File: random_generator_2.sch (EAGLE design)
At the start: 17 parts, among them IC1 OPA2340U

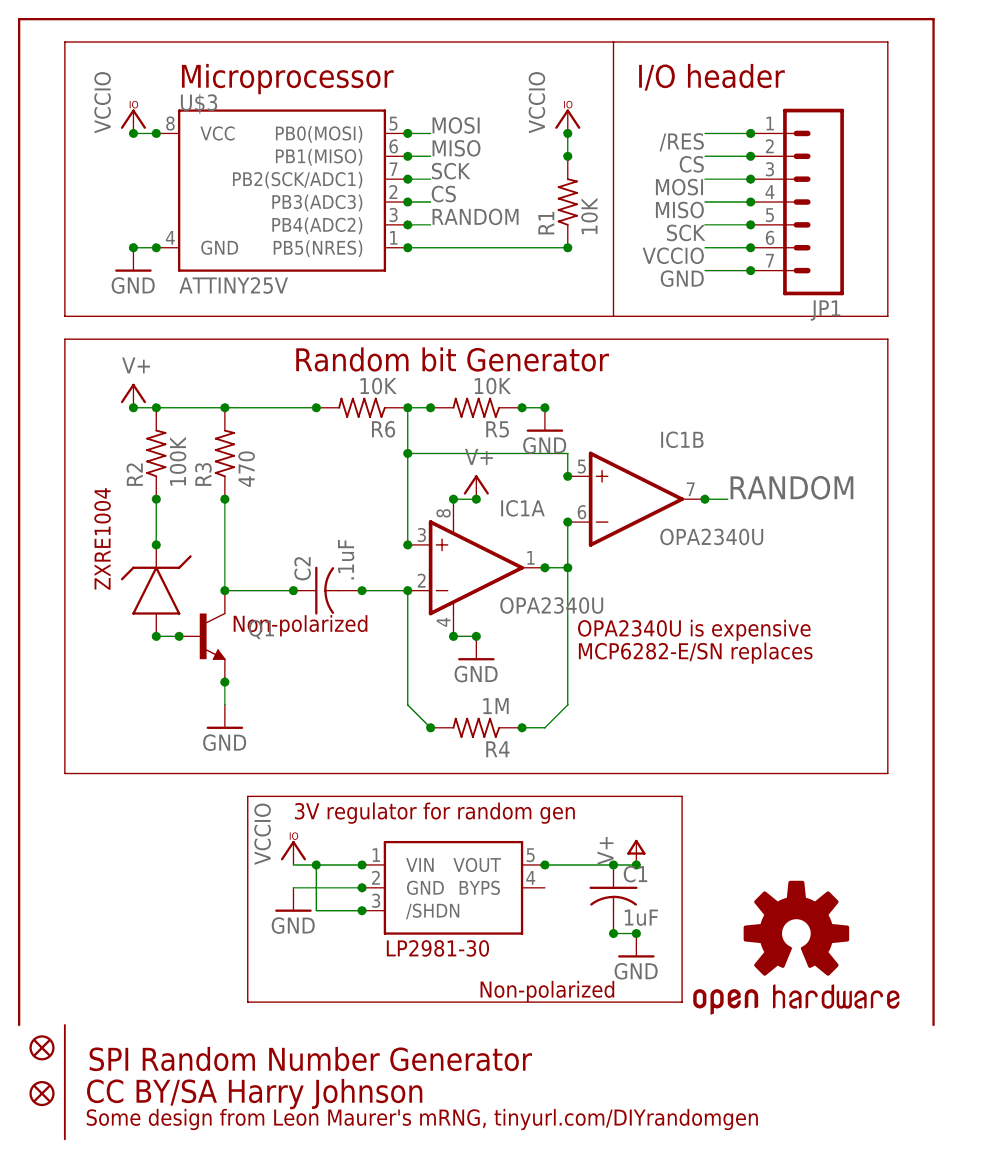
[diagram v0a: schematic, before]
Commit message: MANY BUGS! NOW, HANDLE IT!
A whole nightmarish mess of bugs fixed: Dr Nyquist prescribed some
faster sampling, (just in case). I also tied op amp to VCCIO instead of
3V (for voltage swings guaranteed to trigger logic high), SPI/USI code
now works too. WIll upload an Arduino test program soon…
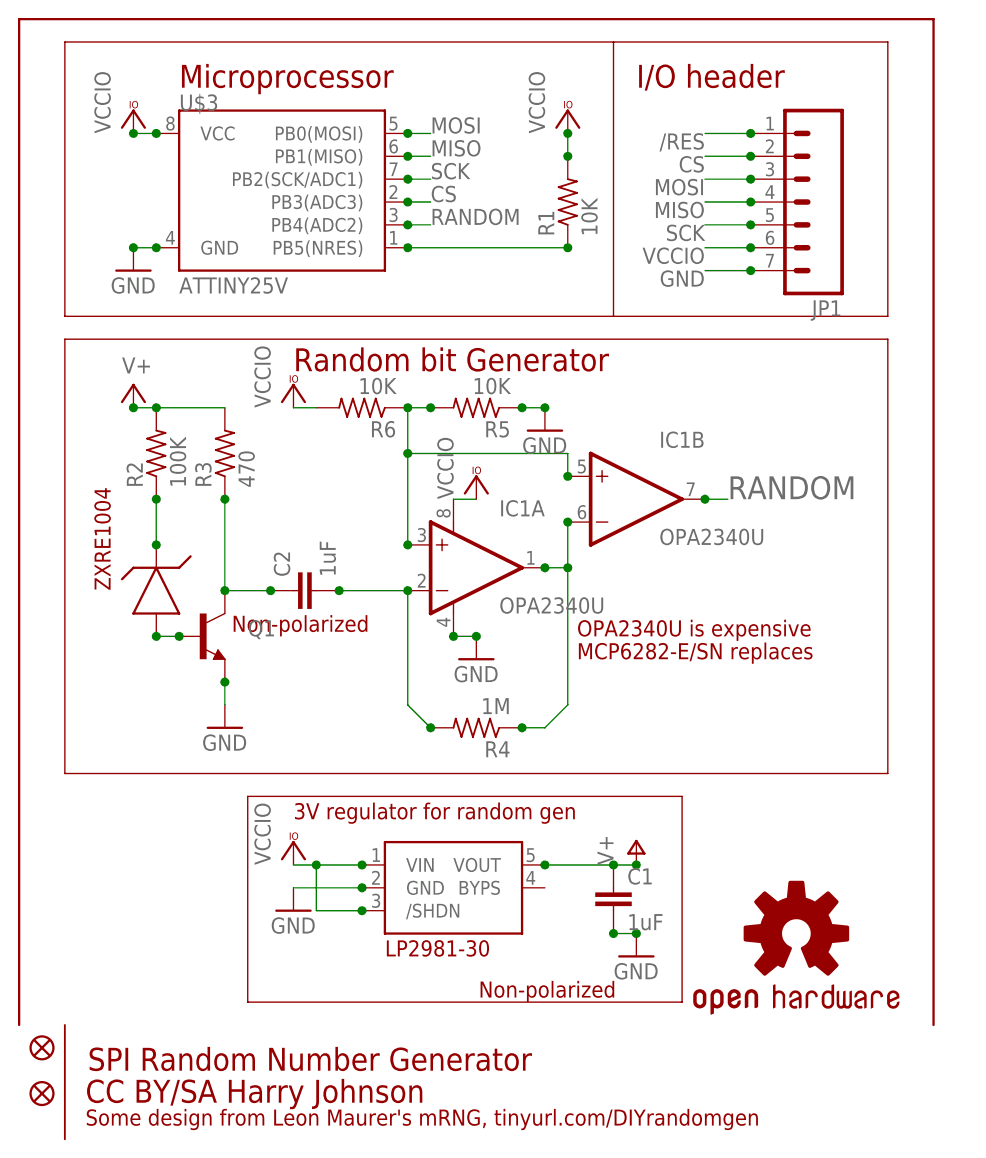
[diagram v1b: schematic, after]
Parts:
- C1: device adafruit:C-USC0805 -> SparkFun:CAP0805
- C2: value .1uF -> 1uF; device adafruit:C-USC0805 -> SparkFun:CAP0805
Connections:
- net V+: no longer IC1A.V+, R6.2
- net VCCIO: now also IC1A.V+, R6.2
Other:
- moved on the sheet: C2
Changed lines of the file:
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@@
 <part name="R5" library="adafruit" deviceset="R-US_" device="R0805" value="10K"/>
 <part name="R6" library="adafruit" deviceset="R-US_" device="R0805" value="10K"/>
-<part name="C2" library="adafruit" deviceset="C-US" device="C0805" value=".1uF"/>
+<part name="C2" library="SparkFun" deviceset="CAP" device="0805" value="1uF"/>
 <part name="SUPPLY1" library="supply2" deviceset="V+" device=""/>
-<part name="SUPPLY2" library="supply2" deviceset="V+" device=""/>
 <part name="U$2" library="hjohnson_library" deviceset="TC1014" device=""/>
-<part name="C1" library="adafruit" deviceset="C-US" device="C0805" value="1uF"/>
+<part name="C1" library="SparkFun" deviceset="CAP" device="0805" value="1uF"/>
 <part name="P+1" library="supply1" deviceset="V+" device=""/>
 <part name="GND1" library="SparkFun" deviceset="GND" device=""/>
@@
 <part name="JP3" library="SparkFun" deviceset="FIDUCIAL" device="UFIDUCIAL"/>
 <part name="U$4" library="SparkFun" deviceset="OSHW-LOGO" device="S"/>
+<part name="VCC4" library="supply1" deviceset="VCCIO" device=""/>
+<part name="VCC5" library="supply1" deviceset="VCCIO" device=""/>
 </parts>
 <sheets>
@@
 <instance part="C2" gate="G$1" x="33.02" y="83.82" rot="R90"/>
 <instance part="SUPPLY1" gate="1" x="12.7" y="106.68"/>
-<instance part="SUPPLY2" gate="1" x="50.8" y="96.52"/>
 <instance part="U$2" gate="G$1" x="45.72" y="48.26"/>
-<instance part="C1" gate="G$1" x="66.04" y="50.8"/>
+<instance part="C1" gate="G$1" x="66.04" y="48.26"/>
 <instance part="P+1" gate="1" x="68.58" y="55.88"/>
 <instance part="GND1" gate="1" x="68.58" y="43.18"/>
@@
 <instance part="JP3" gate="G$1" x="2.54" y="27.94"/>
 <instance part="U$4" gate="G$1" x="86.36" y="45.72"/>
+<instance part="VCC4" gate="G$1" x="30.48" y="106.68"/>
+<instance part="VCC5" gate="G$1" x="50.8" y="96.52"/>
 </instances>
 <busses>
@@
 <wire x1="22.86" y1="93.98" x2="22.86" y2="83.82" width="0.1524" layer="91"/>
 <pinref part="C2" gate="G$1" pin="1"/>
-<wire x1="22.86" y1="83.82" x2="30.48" y2="83.82" width="0.1524" layer="91"/>
+<wire x1="22.86" y1="83.82" x2="27.94" y2="83.82" width="0.1524" layer="91"/>
 <junction x="22.86" y="83.82"/>
-<junction x="30.48" y="83.82"/>
+<junction x="27.94" y="83.82"/>
 <junction x="22.86" y="93.98"/>
 </segment>
@@
 <segment>
 <pinref part="C2" gate="G$1" pin="2"/>
-<wire x1="38.1" y1="83.82" x2="43.18" y2="83.82" width="0.1524" layer="91"/>
+<wire x1="35.56" y1="83.82" x2="43.18" y2="83.82" width="0.1524" layer="91"/>
 <pinref part="R4" gate="G$1" pin="2"/>
 <wire x1="45.72" y1="68.58" x2="43.18" y2="71.12" width="0.1524" layer="91"/>
 <wire x1="43.18" y1="71.12" x2="43.18" y2="83.82" width="0.1524" layer="91"/>
 <junction x="43.18" y="83.82"/>
-<junction x="38.1" y="83.82"/>
+<junction x="35.56" y="83.82"/>
 <pinref part="IC1" gate="A" pin="-IN"/>
 <junction x="45.72" y="68.58"/>
@@
 <pinref part="R3" gate="G$1" pin="2"/>
 <wire x1="15.24" y1="104.14" x2="22.86" y2="104.14" width="0.1524" layer="91"/>
-<pinref part="R6" gate="G$1" pin="2"/>
-<wire x1="22.86" y1="104.14" x2="33.02" y2="104.14" width="0.1524" layer="91"/>
 <pinref part="SUPPLY1" gate="1" pin="V+"/>
 <junction x="15.24" y="104.14"/>
-<junction x="22.86" y="104.14"/>
-<junction x="33.02" y="104.14"/>
 <junction x="12.7" y="104.14"/>
-</segment>
-<segment>
-<pinref part="SUPPLY2" gate="1" pin="V+"/>
-<wire x1="50.8" y1="93.98" x2="48.26" y2="93.98" width="0.1524" layer="91"/>
-<junction x="50.8" y="93.98"/>
-<pinref part="IC1" gate="A" pin="V+"/>
-<junction x="48.26" y="93.98"/>
 </segment>
 <segment>
@@
 <junction x="81.28" y="121.92"/>
 </segment>
-</net>
+<segment>
+<pinref part="VCC4" gate="G$1" pin="VCCIO"/>
+<pinref part="R6" gate="G$1" pin="2"/>
+<wire x1="30.48" y1="104.14" x2="33.02" y2="104.14" width="0.1524" layer="91"/>
+</segment>
+<segment>
+<pinref part="IC1" gate="A" pin="V+"/>
+<pinref part="VCC5" gate="G$1" pin="VCCIO"/>
+<wire x1="48.26" y1="93.98" x2="50.8" y2="93.98" width="0.1524" layer="91"/>
+</segment>
+</net>

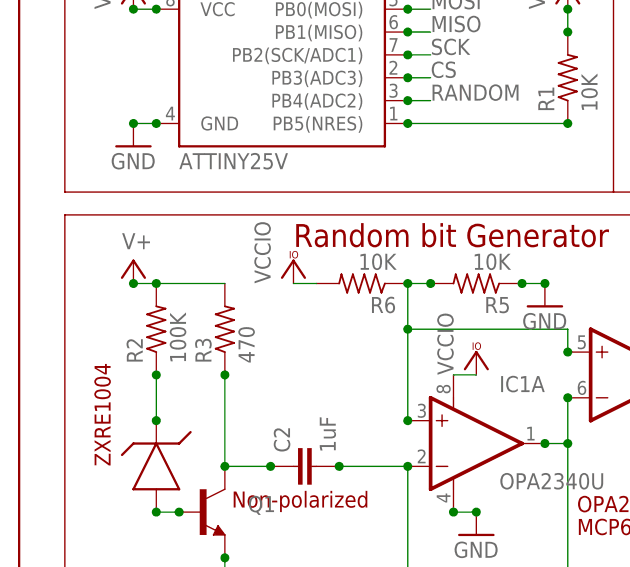
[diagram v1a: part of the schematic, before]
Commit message: Added/fixed comments in firmware, made component designators a bit bigger.
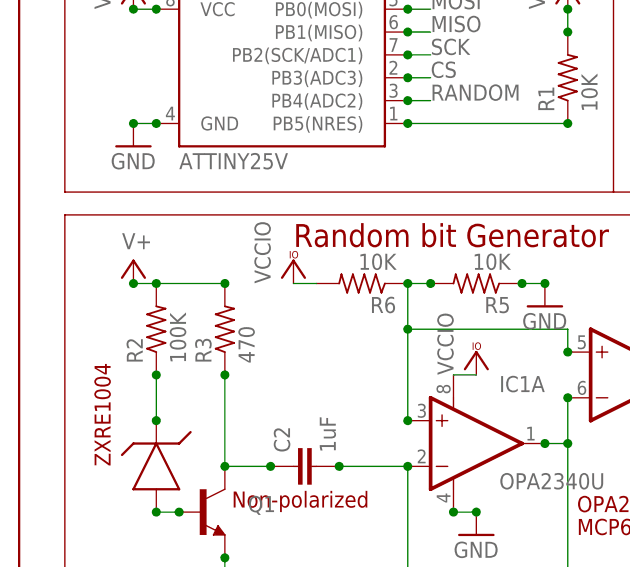
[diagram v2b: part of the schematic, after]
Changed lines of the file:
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@@
 <junction x="15.24" y="104.14"/>
 <junction x="12.7" y="104.14"/>
+<junction x="22.86" y="104.14"/>
 </segment>
 <segment>
